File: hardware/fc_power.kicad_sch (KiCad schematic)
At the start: 41 parts, among them U27 TLV75533PDQNR, U3 LMR51430YFDDCR, U4 LMR51430YFDDCR, U6 LP5912-1.8DRVR, U7 LP5912-3.3DRVR

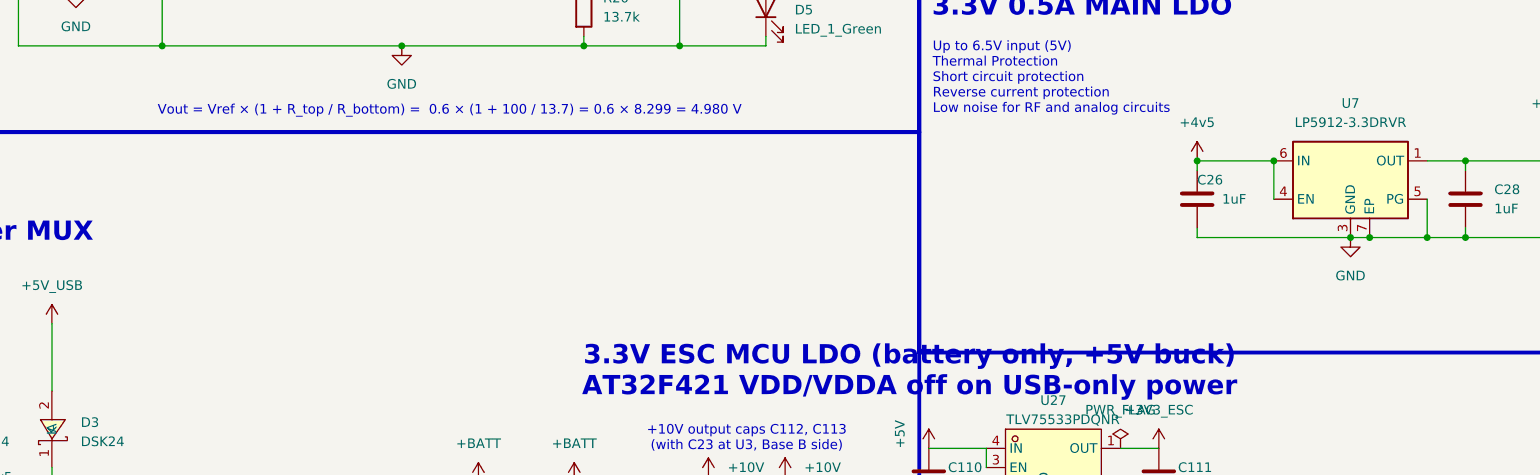
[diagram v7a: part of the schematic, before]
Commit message: One board: merge Base and Core onto the OpenAIO-Whoop 8L HDI stackup
- hardware/OpenAIO.kicad_pcb: the routed Base and Core layouts of 8fa8d7b
  side by side in one board, all routing kept (Core promoted to 8 layers
  before the append so no Base layer was dropped). J90/J91 LGA deleted;
  their 46 nets are now direct links (51 unconnected, listed in
  research/ROUTING.md). Stackup and board setup from OpenAIO-Whoop:
  8L HDI 1+6+1, 0.997 mm, 1 oz all layers, microvia 0.25/0.10,
  buried 0.33/0.15. Base DRC severities and exclusions kept.
- hardware/OpenAIO.kicad_dru: canonical block, Whoop HDI via rules,
  Base/Core rules that still apply; LGA, 2 oz and 1.6 mm via rules gone.
- Schematic: core_interface sheet removed; DPS368 baro U28 on I2C0;
  review fixes (U3 HF cap C116, RP2354 caps C117/C118, buzzer flyback D10,
  SD card on +3.3V, D9 on +4v5, FLASH_CS -> SD_CS, PWR_FLAGs, U7 pin
  names, ESC cap pin types, L4 LCSC). ERC 32 -> 0 errors.
- Libraries project-local: every footprint, 3D model and symbol in lib;
  OPENDRONE_LIB aliases removed from the lib tables.
- Two-board projects, multiboard config and LGA tools removed; Whoop
  board tools added in hardware/tools.
- Docs: README, AGENTS.md, research/ROUTING.md (hand-over),
  SCHEMATIC-REVIEW-2026-10-15.md, Betaflight target baro.

DRC: 38 errors (25 dangling LGA escape vias, 13 Core leftovers listed),
51 unconnected (the Base-Core links), 0 net or value parity issues.

Co-Authored-By: Claude Opus 5.5 <noreply@anthropic.com>
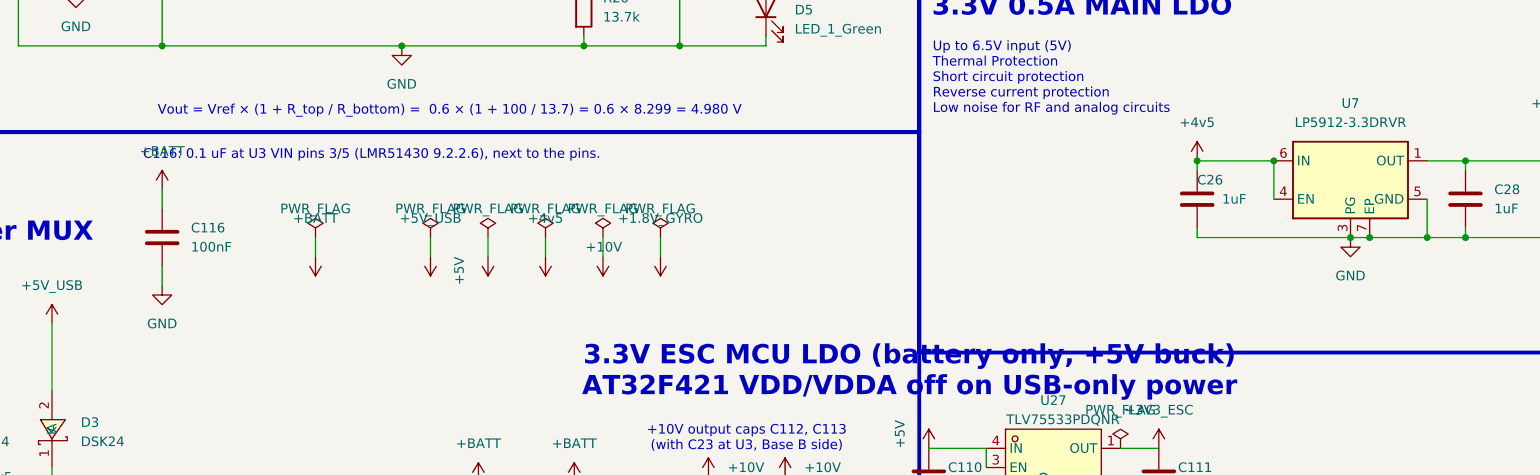
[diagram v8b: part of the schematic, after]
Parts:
- added C116: 100nF, lib:C_0402_1005Metric, symbol Device:C
- C102, C103, C18, C19: footprint Capacitor_SMD:C_0805_2012Metric -> lib:C_0805_2012Metric
- C105, C106: footprint Capacitor_SMD:C_1206_3216Metric -> lib:C_1206_3216Metric
- C107, C25, C26, C27, C28: footprint Capacitor_SMD:C_0402_1005Metric -> lib:C_0402_1005Metric
- C110, C111, C20, C21: footprint Capacitor_SMD:C_0201_0603Metric -> lib:C_0201_0603Metric
- C112, C113, C23, C24: footprint Capacitor_SMD:C_0603_1608Metric -> lib:C_0603_1608Metric
- D4, D5, D6, D7: footprint LED_SMD:LED_0402_1005Metric -> lib:LED_0402_1005Metric; MPN XL-1005UGC -> XL-1005UGC
- R17, R18, R19, R20, R21, R22, R23, R24: footprint Resistor_SMD:R_0201_0603Metric -> lib:R_0201_0603Metric
- TP30: footprint TestPoint:TestPoint_Pad_D1.0mm -> lib:TestPoint_Pad_D1.0mm
- U27: footprint OpenRX-Shared:X2SON-4_L1.0-W1.0-P0.65-TL-EP -> lib:X2SON-4_L1.0-W1.0-P0.65-TL-EP; symbol OpenRX-Shared:TLV75533PDQNR -> lib:TLV75533PDQNR
- U7: footprint Package_SON:WSON-6-1EP_2x2mm_P0.65mm_EP1x1.6mm -> lib:WSON-6-1EP_2x2mm_P0.65mm_EP1x1.6mm; symbol Regulator_Linear:LP5912-3.3DRV -> lib:LP5912-3.3DRV_1
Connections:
- net +BATT: now also C116.1
- net GND: now also C116.2
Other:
- note added: "C116: 0.1 uF at U3 VIN pins 3/5 (LMR51430 9.2.2.6), next to the pins."
